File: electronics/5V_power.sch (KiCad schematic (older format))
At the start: 7 parts, among them P4 CONN_01X02, P5 CONN_01X02, U1 LM2576T-5

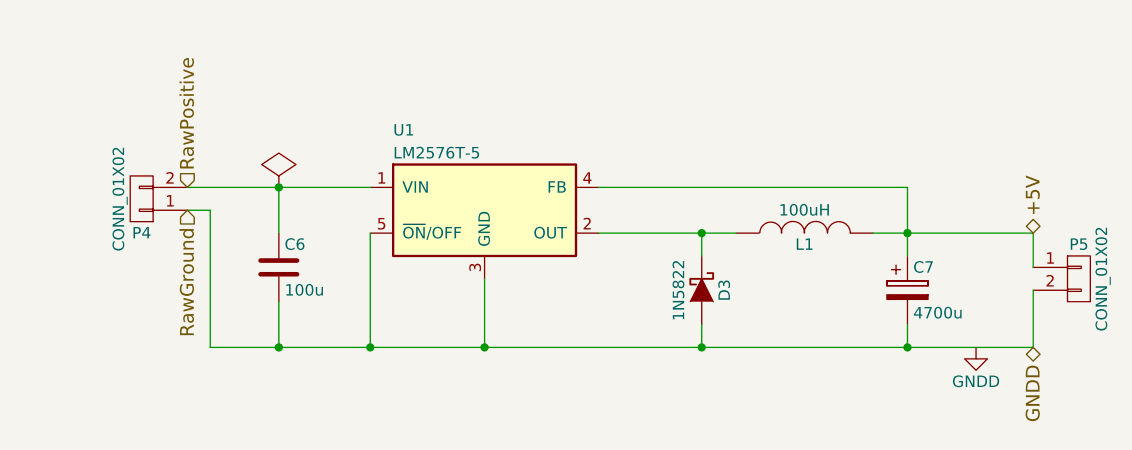
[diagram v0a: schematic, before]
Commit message: input board -> mosfet in place of triak
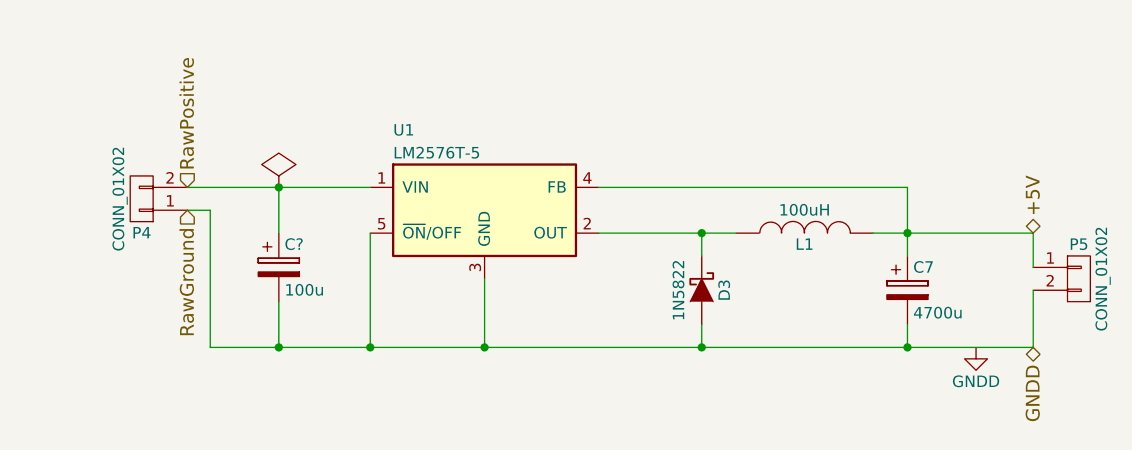
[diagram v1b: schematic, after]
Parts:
- removed C6: 100u, symbol C
- added C?: 100u, symbol CP
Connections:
- net GNDD: now also C?.2
- net RawPositive: now also C?.1
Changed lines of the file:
@@
-$EndComp
-$Comp
-L C C6
-U 1 1 55EBFAD5
-P 2000 1500
-F 0 "C6" H 2025 1600 50  0000 L CNN
-F 1 "100u" H 2025 1400 50  0000 L CNN
-F 2 "" H 2038 1350 30  0000 C CNN
-F 3 "" H 2000 1500 60  0000 C CNN
-	1    2000 1500
-	1    0    0    -1
 $EndComp
 $Comp
@@
 Text HLabel 5300 1850 3    60   BiDi ~ 0
 GNDD
+$Comp
+L CP C?
+U 1 1 55EC1B11
+P 2000 1500
+F 0 "C?" H 2025 1600 50  0000 L CNN
+F 1 "100u" H 2025 1400 50  0000 L CNN
+F 2 "" H 2038 1350 30  0000 C CNN
+F 3 "" H 2000 1500 60  0000 C CNN
+	1    2000 1500
+	1    0    0    -1
+$EndComp
 $EndSCHEMATC

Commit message: input protection: crowbar + power on switch
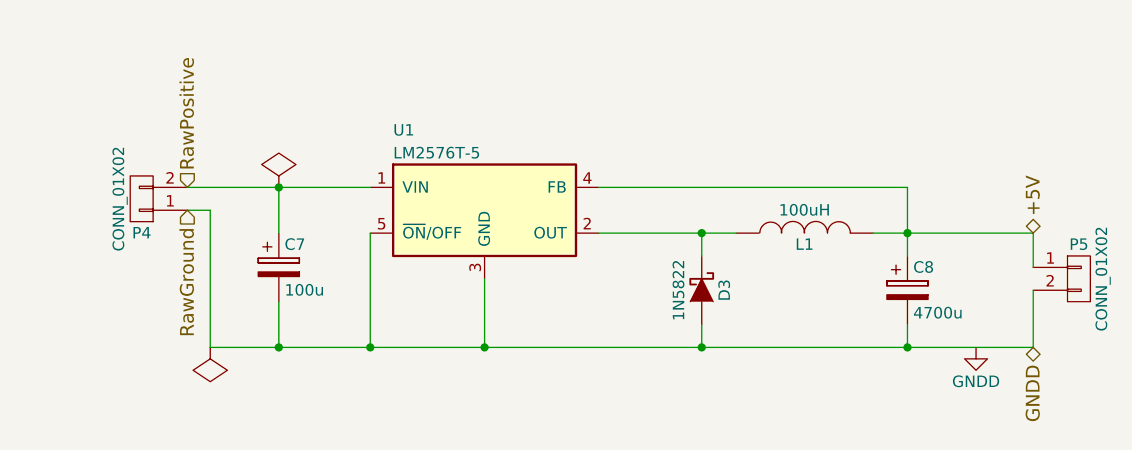
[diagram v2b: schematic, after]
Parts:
- gave numbers to parts that had none: 1
- renumbered C7 to C8
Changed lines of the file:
@@
 $EndComp
 $Comp
-L CP C7
+L CP C8
 U 1 1 55EBFB83
 P 4750 1600
-F 0 "C7" H 4775 1700 50  0000 L CNN
+F 0 "C8" H 4775 1700 50  0000 L CNN
 F 1 "4700u" H 4775 1500 50  0000 L CNN
 F 2 "" H 4788 1450 30  0000 C CNN
@@
 GNDD
 $Comp
-L CP C?
+L CP C7
 U 1 1 55EC1B11
 P 2000 1500
-F 0 "C?" H 2025 1600 50  0000 L CNN
+F 0 "C7" H 2025 1600 50  0000 L CNN
 F 1 "100u" H 2025 1400 50  0000 L CNN
 F 2 "" H 2038 1350 30  0000 C CNN
@@
 	1    0    0    -1
 $EndComp
+$Comp
+L PWR_FLAG #FLG015
+U 1 1 566DC612
+P 1700 1850
+F 0 "#FLG015" H 1700 1945 50  0001 C CNN
+F 1 "PWR_FLAG" H 1700 2030 50  0001 C CNN
+F 2 "" H 1700 1850 60  0000 C CNN
+F 3 "" H 1700 1850 60  0000 C CNN
+	1    1700 1850
+	-1   0    0    1
+$EndComp
 $EndSCHEMATC

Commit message: resigned from using hall effect current sensor
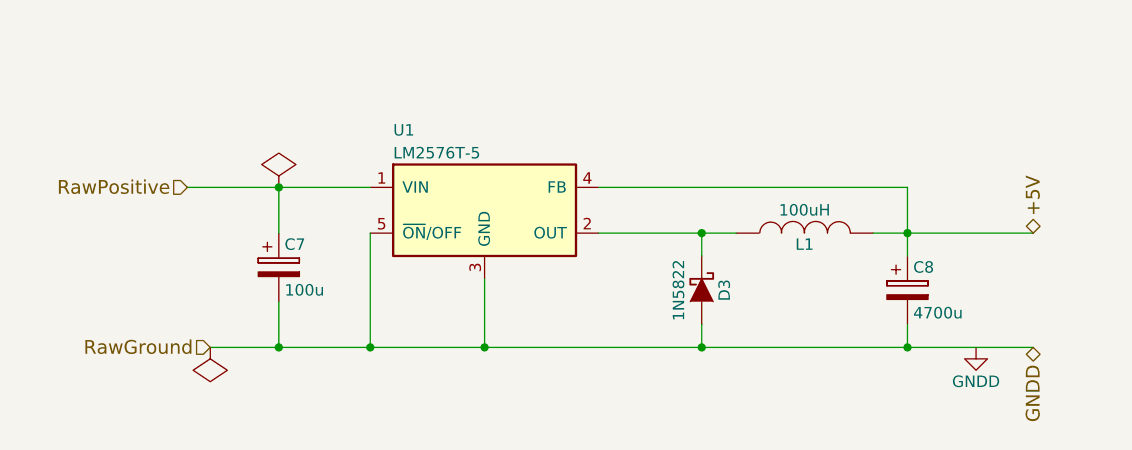
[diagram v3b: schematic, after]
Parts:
- removed P4, P5: CONN_01X02, symbol CONN_01X02
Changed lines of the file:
@@
 Comment4 ""
 $EndDescr
-$Comp
-L CONN_01X02 P4
-U 1 1 55EBF475
-P 1400 1200
-F 0 "P4" H 1400 1350 50  0000 C CNN
-F 1 "CONN_01X02" V 1500 1200 50  0000 C CNN
-F 2 "" H 1400 1200 60  0000 C CNN
-F 3 "" H 1400 1200 60  0000 C CNN
-	1    1400 1200
-	-1   0    0    1
-$EndComp
-Text HLabel 1600 1150 1    60   Input ~ 0
+Text HLabel 1600 1150 0    60   Input ~ 0
 RawPositive
-Text HLabel 1600 1250 3    60   Input ~ 0
+Text HLabel 1700 1850 0    60   Input ~ 0
 RawGround
 $Comp
@@
 Wire Wire Line
 	1600 1150 2400 1150
-Wire Wire Line
-	1600 1250 1700 1250
-Wire Wire Line
-	1700 1250 1700 1850
 Wire Wire Line
 	2000 1650 2000 1850
@@
 	1    0    0    -1
 $EndComp
-$Comp
-L CONN_01X02 P5
-U 1 1 55EC08D2
-P 5500 1550
-F 0 "P5" H 5500 1700 50  0000 C CNN
-F 1 "CONN_01X02" V 5600 1550 50  0000 C CNN
-F 2 "" H 5500 1550 60  0000 C CNN
-F 3 "" H 5500 1550 60  0000 C CNN
-	1    5500 1550
-	1    0    0    -1
-$EndComp
-Wire Wire Line
-	5300 1350 5300 1500
-Wire Wire Line
-	5300 1850 5300 1600
 Text HLabel 5300 1350 1    60   BiDi ~ 0
 +5V

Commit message: redoing power supply as an 5A one
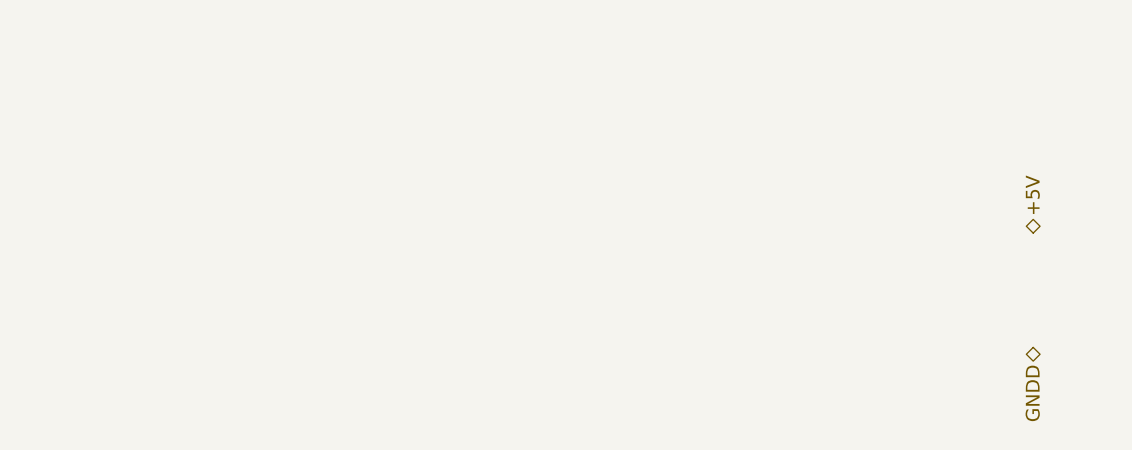
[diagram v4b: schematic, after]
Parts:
- removed C7: 100u, symbol CP
- removed C8: 4700u, symbol CP
- removed D3: 1N5822, symbol D_Schottky
- removed L1: 100uH, symbol INDUCTOR
- removed U1: LM2576T-5, TO-220-5, symbol LM2576T-5
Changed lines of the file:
@@
 $Descr A4 11693 8268
 encoding utf-8
-Sheet 3 3
+Sheet 2 3
 Title ""
 Date ""
@@
 Comment4 ""
 $EndDescr
-Text HLabel 1600 1150 0    60   Input ~ 0
-RawPositive
-Text HLabel 1700 1850 0    60   Input ~ 0
-RawGround
-$Comp
-L LM2576T-5 U1
-U 1 1 55EBF9BF
-P 2900 1250
-F 0 "U1" H 2500 1600 50  0000 L CNN
-F 1 "LM2576T-5" H 2500 1500 50  0000 L CNN
-F 2 "TO-220-5" H 3200 1000 50  0001 C CIN
-F 3 "http://electropark.pl/attachment.php?id_attachment=170" H 2900 1250 50  0001 C CNN
-	1    2900 1250
-	1    0    0    -1
-$EndComp
-$Comp
-L CP C8
-U 1 1 55EBFB83
-P 4750 1600
-F 0 "C8" H 4775 1700 50  0000 L CNN
-F 1 "4700u" H 4775 1500 50  0000 L CNN
-F 2 "" H 4788 1450 30  0000 C CNN
-F 3 "" H 4750 1600 60  0000 C CNN
-	1    4750 1600
-	1    0    0    -1
-$EndComp
-$Comp
-L D_Schottky D3
-U 1 1 55EBFCEF
-P 3850 1600
-F 0 "D3" H 3850 1700 50  0000 C CNN
-F 1 "1N5822" H 3850 1500 50  0000 C CNN
-F 2 "" H 3850 1600 60  0000 C CNN
-F 3 "http://www.mouser.com/ds/2/389/CD00001626-249576.pdf" H 3850 1600 60  0001 C CNN
-	1    3850 1600
-	0    1    1    0
-$EndComp
-$Comp
-L INDUCTOR L1
-U 1 1 55EBFD54
-P 4300 1350
-F 0 "L1" V 4250 1350 50  0000 C CNN
-F 1 "100uH" V 4400 1350 50  0000 C CNN
-F 2 "" H 4300 1350 60  0000 C CNN
-F 3 "" H 4300 1350 60  0000 C CNN
-	1    4300 1350
-	0    -1   -1   0
-$EndComp
-Wire Wire Line
-	1600 1150 2400 1150
-Wire Wire Line
-	2000 1650 2000 1850
-Wire Wire Line
-	2900 1850 2900 1550
-Wire Wire Line
-	2400 1850 2400 1350
-Wire Wire Line
-	1700 1850 5300 1850
-Connection ~ 2400 1850
-Connection ~ 2000 1850
-Wire Wire Line
-	4600 1350 5300 1350
-Wire Wire Line
-	4750 1150 4750 1450
-Wire Wire Line
-	4750 1150 3400 1150
-Wire Wire Line
-	3850 1850 3850 1750
-Connection ~ 2900 1850
-Connection ~ 3850 1850
-Connection ~ 4750 1850
-Wire Wire Line
-	2000 1350 2000 1150
-Connection ~ 2000 1150
-Wire Wire Line
-	4000 1350 3400 1350
-Wire Wire Line
-	3850 1450 3850 1350
-Connection ~ 3850 1350
-Wire Wire Line
-	4750 1750 4750 1850
-Connection ~ 4750 1350
-$Comp
-L PWR_FLAG #FLG013
-U 1 1 55EC042D
-P 2000 1150
-F 0 "#FLG013" H 2000 1245 50  0001 C CNN
-F 1 "PWR_FLAG" H 2000 1330 50  0001 C CNN
-F 2 "" H 2000 1150 60  0000 C CNN
-F 3 "" H 2000 1150 60  0000 C CNN
-	1    2000 1150
-	1    0    0    -1
-$EndComp
-$Comp
-L GNDD #PWR014
-U 1 1 55EC0609
-P 5050 1850
-F 0 "#PWR014" H 5050 1600 50  0001 C CNN
-F 1 "GNDD" H 5050 1700 50  0000 C CNN
-F 2 "" H 5050 1850 60  0000 C CNN
-F 3 "" H 5050 1850 60  0000 C CNN
-	1    5050 1850
-	1    0    0    -1
-$EndComp
 Text HLabel 5300 1350 1    60   BiDi ~ 0
 +5V
 Text HLabel 5300 1850 3    60   BiDi ~ 0
 GNDD
-$Comp
-L CP C7
-U 1 1 55EC1B11
-P 2000 1500
-F 0 "C7" H 2025 1600 50  0000 L CNN
-F 1 "100u" H 2025 1400 50  0000 L CNN
-F 2 "" H 2038 1350 30  0000 C CNN
-F 3 "" H 2000 1500 60  0000 C CNN
-	1    2000 1500
-	1    0    0    -1
-$EndComp
-$Comp
-L PWR_FLAG #FLG015
-U 1 1 566DC612
-P 1700 1850
-F 0 "#FLG015" H 1700 1945 50  0001 C CNN
-F 1 "PWR_FLAG" H 1700 2030 50  0001 C CNN
-F 2 "" H 1700 1850 60  0000 C CNN
-F 3 "" H 1700 1850 60  0000 C CNN
-	1    1700 1850
-	-1   0    0    1
-$EndComp
 $EndSCHEMATC
